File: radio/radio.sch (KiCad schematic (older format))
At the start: 0 parts

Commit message: pushing end-of-workday changes to radio module
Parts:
- added U?: SC18IS602, Housings_SSOP:TSSOP-16_4.4x5mm_Pitch0.65mm, symbol star-common-lib:SC18IS602
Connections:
- net RFM69HCW/MISO: now also U?.5 (MISO)
- net RFM69HCW/MOSI: now also U?.6 (MOSI)
- net RFM69HCW/SCK: now also U?.11 (SPICLK)
- net RFM69HCW/nSS: now also U?.1 (GPIO0)
- new net +3V3: U?.12 (VDD)
- new net GND: U?.14 (A0), U?.15 (A1), U?.16 (A2), U?.4 (VSS)
- no-connect marks 0 -> 4
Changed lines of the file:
@@
 F8 "SCK" I L 2650 2450 50
 $EndSheet
+$Comp
+L star-common-lib:SC18IS602 U?
+U 1 1 5E5B9427
+P 3000 3550
+F 0 "U?" H 3000 4215 50  0000 C CNN
+F 1 "SC18IS602" H 3000 4124 50  0000 C CNN
+F 2 "Housings_SSOP:TSSOP-16_4.4x5mm_Pitch0.65mm" H 3000 4033 50  0000 C CNN
+F 3 "" H 3050 4000 50  0001 C CNN
+	1    3000 3550
+	1    0    0    -1
+$EndComp
+Wire Wire Line
+	3550 3700 4300 3700
+Wire Wire Line
+	4300 3700 4300 4600
+Wire Wire Line
+	4300 4600 2000 4600
+Wire Wire Line
+	2000 4600 2000 2450
+Wire Wire Line
+	2000 2450 2650 2450
+Wire Wire Line
+	2450 3200 2350 3200
+$Comp
+L power:+3.3V #PWR?
+U 1 1 5E5BB3BC
+P 4500 3600
+F 0 "#PWR?" H 4500 3450 50  0001 C CNN
+F 1 "+3.3V" H 4515 3773 50  0000 C CNN
+F 2 "" H 4500 3600 50  0001 C CNN
+F 3 "" H 4500 3600 50  0001 C CNN
+	1    4500 3600
+	1    0    0    -1
+$EndComp
+$Comp
+L power:GND #PWR?
+U 1 1 5E5BC8F7
+P 1900 3500
+F 0 "#PWR?" H 1900 3250 50  0001 C CNN
+F 1 "GND" H 1905 3327 50  0000 C CNN
+F 2 "" H 1900 3500 50  0001 C CNN
+F 3 "" H 1900 3500 50  0001 C CNN
+	1    1900 3500
+	1    0    0    -1
+$EndComp
+Wire Wire Line
+	2450 3600 2300 3600
+Wire Wire Line
+	2300 3600 2300 2250
+Wire Wire Line
+	2300 2250 2650 2250
+Wire Wire Line
+	2650 2350 2250 2350
+Wire Wire Line
+	2250 2350 2250 3700
+Wire Wire Line
+	2250 3700 2450 3700
+Wire Wire Line
+	1900 3500 2450 3500
+Wire Wire Line
+	2650 2150 2350 2150
+Wire Wire Line
+	2350 2150 2350 3200
+Wire Wire Line
+	3550 3600 4500 3600
+$Comp
+L power:GND #PWR?
+U 1 1 5E5C0384
+P 4000 3400
+F 0 "#PWR?" H 4000 3150 50  0001 C CNN
+F 1 "GND" H 4005 3227 50  0000 C CNN
+F 2 "" H 4000 3400 50  0001 C CNN
+F 3 "" H 4000 3400 50  0001 C CNN
+	1    4000 3400
+	1    0    0    -1
+$EndComp
+Wire Wire Line
+	3550 3400 4000 3400
+Wire Wire Line
+	3550 3300 4000 3300
+Wire Wire Line
+	4000 3300 4000 3400
+Connection ~ 4000 3400
+Wire Wire Line
+	3550 3200 4000 3200
+Wire Wire Line
+	4000 3200 4000 3300
+Connection ~ 4000 3300
+NoConn ~ 3650 3500
+NoConn ~ 3650 3800
+NoConn ~ 2350 3300
+NoConn ~ 2350 3400
+Wire Wire Line
+	3650 3500 3550 3500
+Wire Wire Line
+	3650 3800 3550 3800
+Wire Wire Line
+	2350 3300 2450 3300
+Wire Wire Line
+	2350 3400 2450 3400
 $EndSCHEMATC

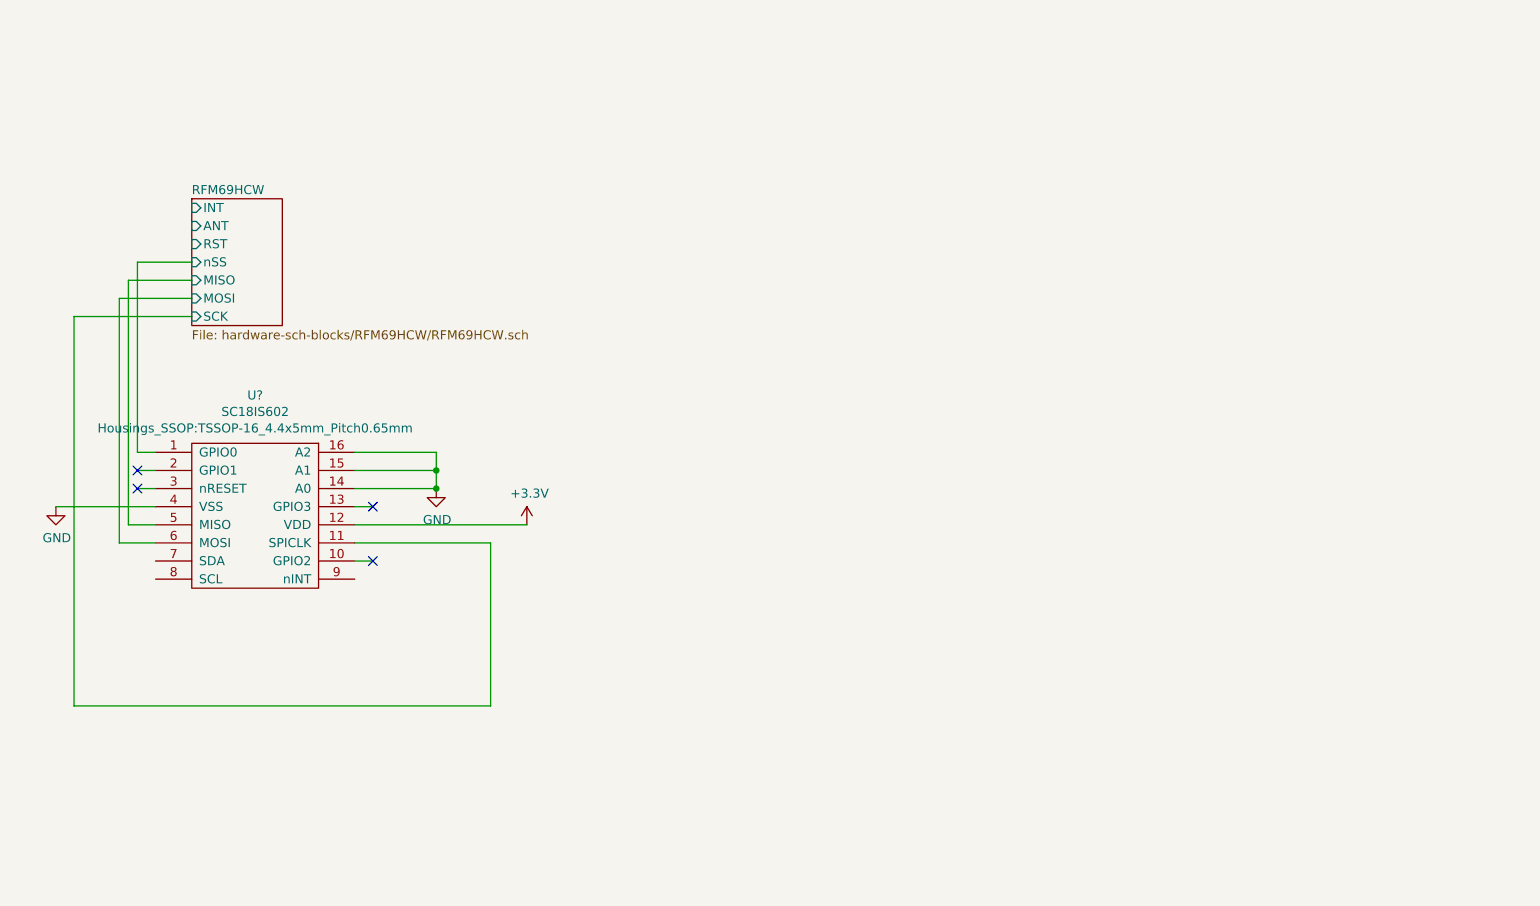
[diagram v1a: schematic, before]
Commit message: add CAM interconnects
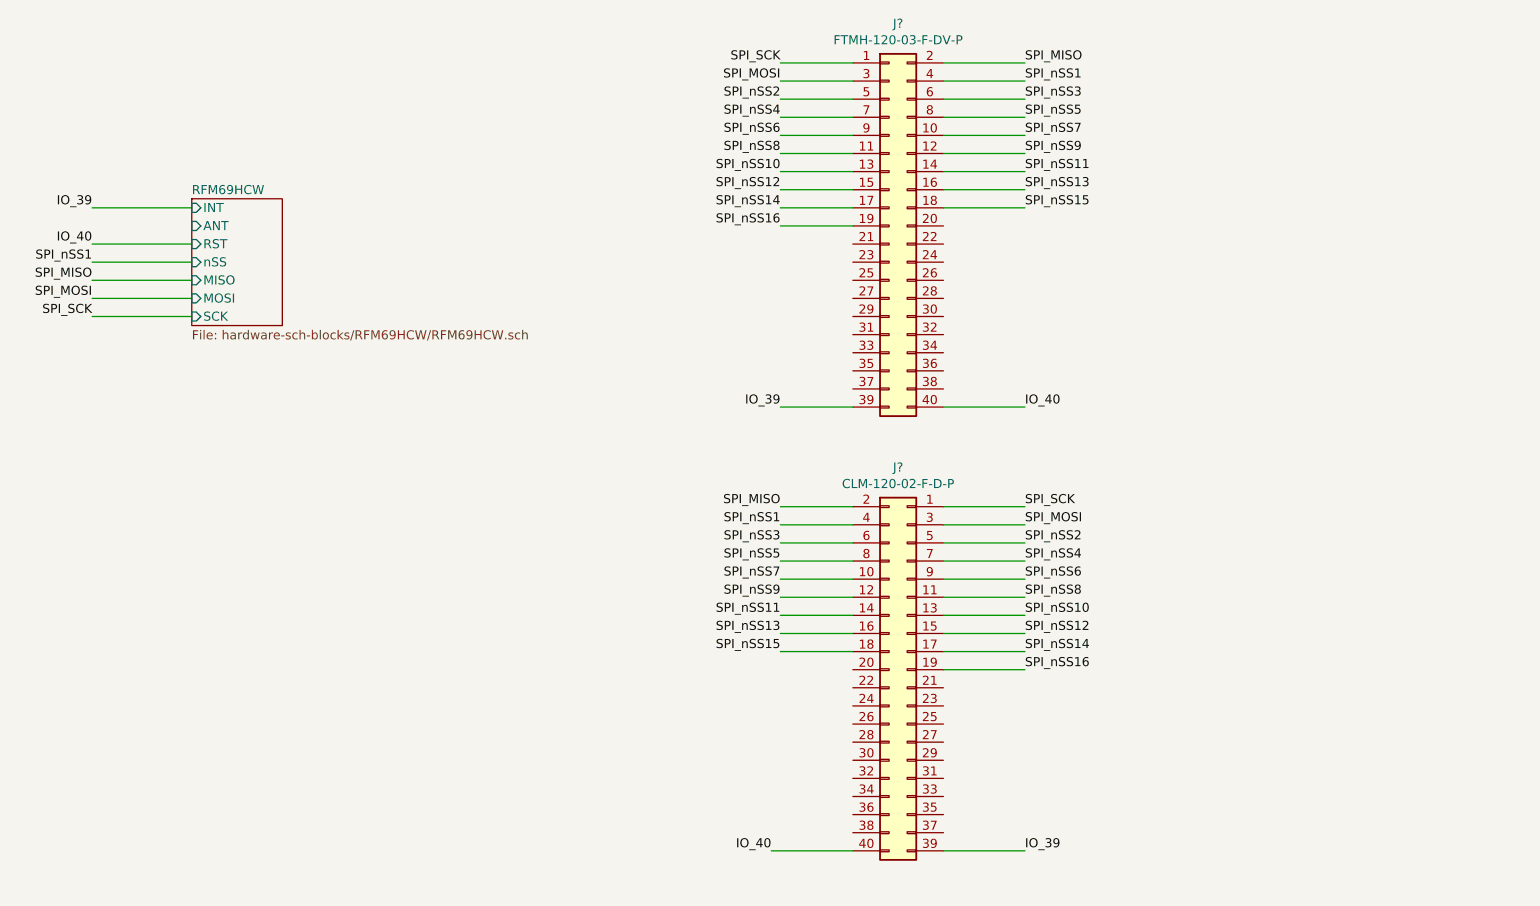
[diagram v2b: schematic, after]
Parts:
- removed U?: SC18IS602, Housings_SSOP:TSSOP-16_4.4x5mm_Pitch0.65mm, symbol star-common-lib:SC18IS602
- added J?: FTMH-120-03-F-DV-P, symbol star-common-lib:FTMH-120-03-F-DV-P
- added J?: CLM-120-02-F-D-P, symbol star-common-lib:CLM-120-02-F-D-P
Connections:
- new net IO_39: J?.39 (Pin_39), J?.39 (Pin_39)
- new net IO_40: J?.40 (Pin_40), J?.40 (Pin_40)
- new net SPI_MISO: J?.2 (Pin_2), J?.2 (Pin_2)
- new net SPI_MOSI: J?.3 (Pin_3), J?.3 (Pin_3)
- new net SPI_SCK: J?.1 (Pin_1), J?.1 (Pin_1)
- new net SPI_nSS1: J?.4 (Pin_4), J?.4 (Pin_4)
- new net SPI_nSS10: J?.13 (Pin_13), J?.13 (Pin_13)
- new net SPI_nSS11: J?.14 (Pin_14), J?.14 (Pin_14)
- new net SPI_nSS12: J?.15 (Pin_15), J?.15 (Pin_15)
- new net SPI_nSS13: J?.16 (Pin_16), J?.16 (Pin_16)
- new net SPI_nSS14: J?.17 (Pin_17), J?.17 (Pin_17)
- new net SPI_nSS15: J?.18 (Pin_18), J?.18 (Pin_18)
- new net SPI_nSS16: J?.19 (Pin_19), J?.19 (Pin_19)
- new net SPI_nSS2: J?.5 (Pin_5), J?.5 (Pin_5)
- new net SPI_nSS3: J?.6 (Pin_6), J?.6 (Pin_6)
- new net SPI_nSS4: J?.7 (Pin_7), J?.7 (Pin_7)
- new net SPI_nSS5: J?.8 (Pin_8), J?.8 (Pin_8)
- new net SPI_nSS6: J?.9 (Pin_9), J?.9 (Pin_9)
- new net SPI_nSS7: J?.10 (Pin_10), J?.10 (Pin_10)
- new net SPI_nSS8: J?.11 (Pin_11), J?.11 (Pin_11)
- new net SPI_nSS9: J?.12 (Pin_12), J?.12 (Pin_12)
- no-connect marks 4 -> 0
